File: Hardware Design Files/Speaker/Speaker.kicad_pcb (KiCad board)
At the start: 2 copper layers, 40.2 x 36.1 mm, 22 parts, among them J1 D7-D0, J2 CLK DAC1 DAC2 PRE_AMP SPKR+ S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, J3 SPKR- SPKR+ 3V3 GND 5V D3V3 D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, U1 LMV358IDR, U2 MAX5187BEEG+, U3 PAM8304, U4 PAM8304, U5 PAM8304

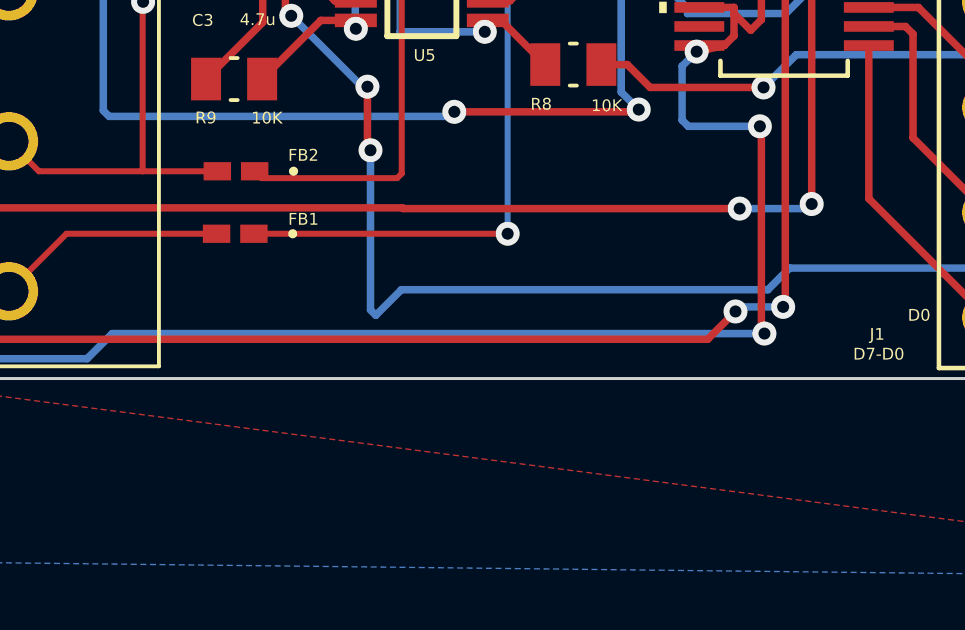
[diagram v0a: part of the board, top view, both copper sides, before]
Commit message: added label to pcb
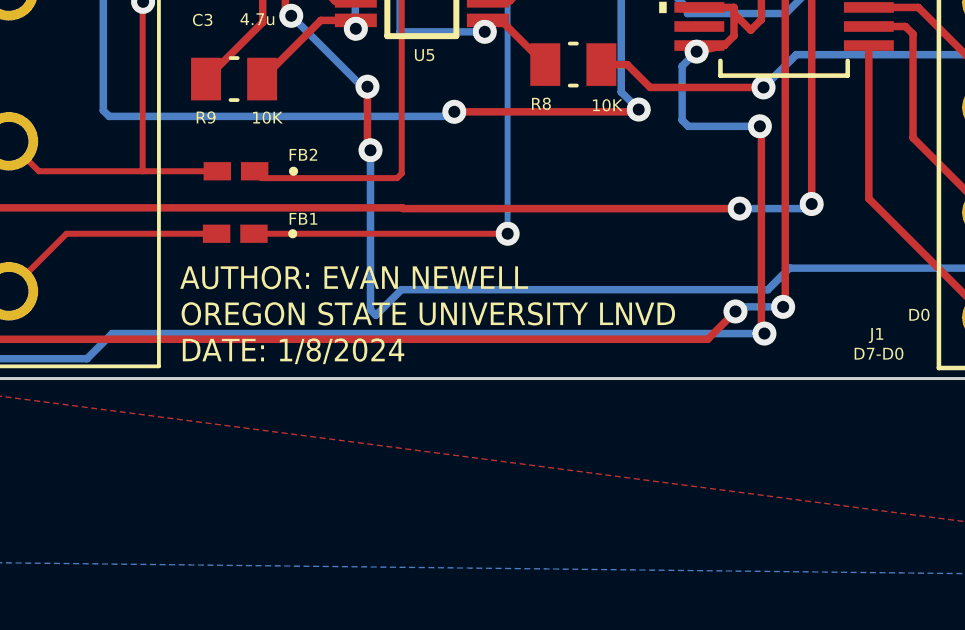
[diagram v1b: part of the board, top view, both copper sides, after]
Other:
- board text added: "AUTHOR: EVAN NEWELL OREGON STATE UNIVERSITY LNVD DATE: 1/8/2024"
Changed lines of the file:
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@@
     (effects (font (size 0.393701 0.393701) (thickness 0.098425)))
+  )
+  (gr_text "AUTHOR: EVAN NEWELL\nOREGON STATE UNIVERSITY LNVD\nDATE: 1/8/2024" (at 98.5012 119.253) (layer "F.SilkS")
+    (effects (font (size 0.75 0.7) (thickness 0.15)) (justify left bottom))
   )
   (gr_text "D7" (at 123.0884 93.2942) (layer "F.SilkS")
